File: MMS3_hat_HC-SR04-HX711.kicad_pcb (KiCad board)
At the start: 2 copper layers, 100 x 50 mm, 64 parts, among them J1 Chainbus in, J10 Conn_01x04_Pin, J11 Conn_01x04_Pin, J2 Chainbus Out, J3 Conn_01x04_Pin, J4 Debug_USART_TX, J5 Conn_01x04_Pin, J6 Conn_01x04_Pin, J7 Program, J8 Conn_01x04_Pin, J9 Conn_01x04_Pin, Q1 MMBT3906, U1 SN74CB3Q3384APW, U2 M24C64, U3 AMS1117, U4 CH32V003FxPx, U5 HX711

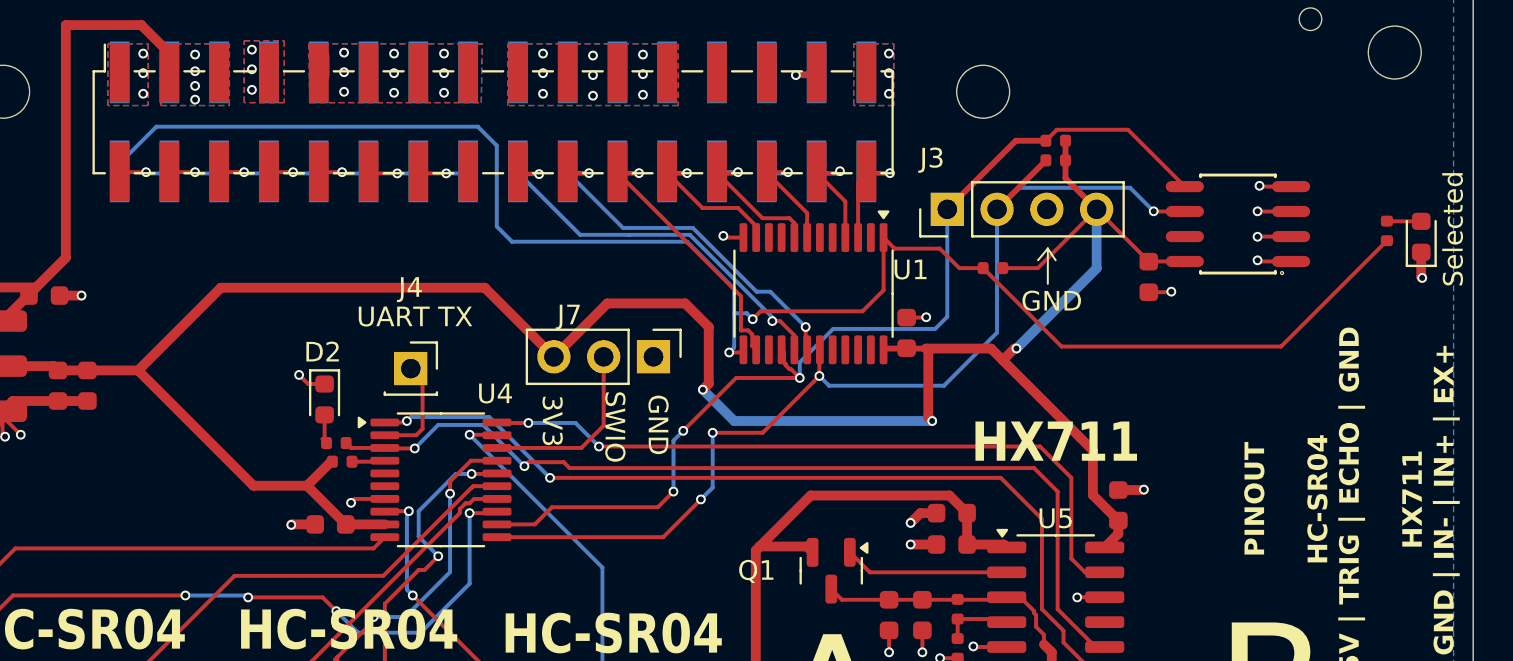
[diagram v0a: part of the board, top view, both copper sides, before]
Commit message: updated bus switch to sensible one
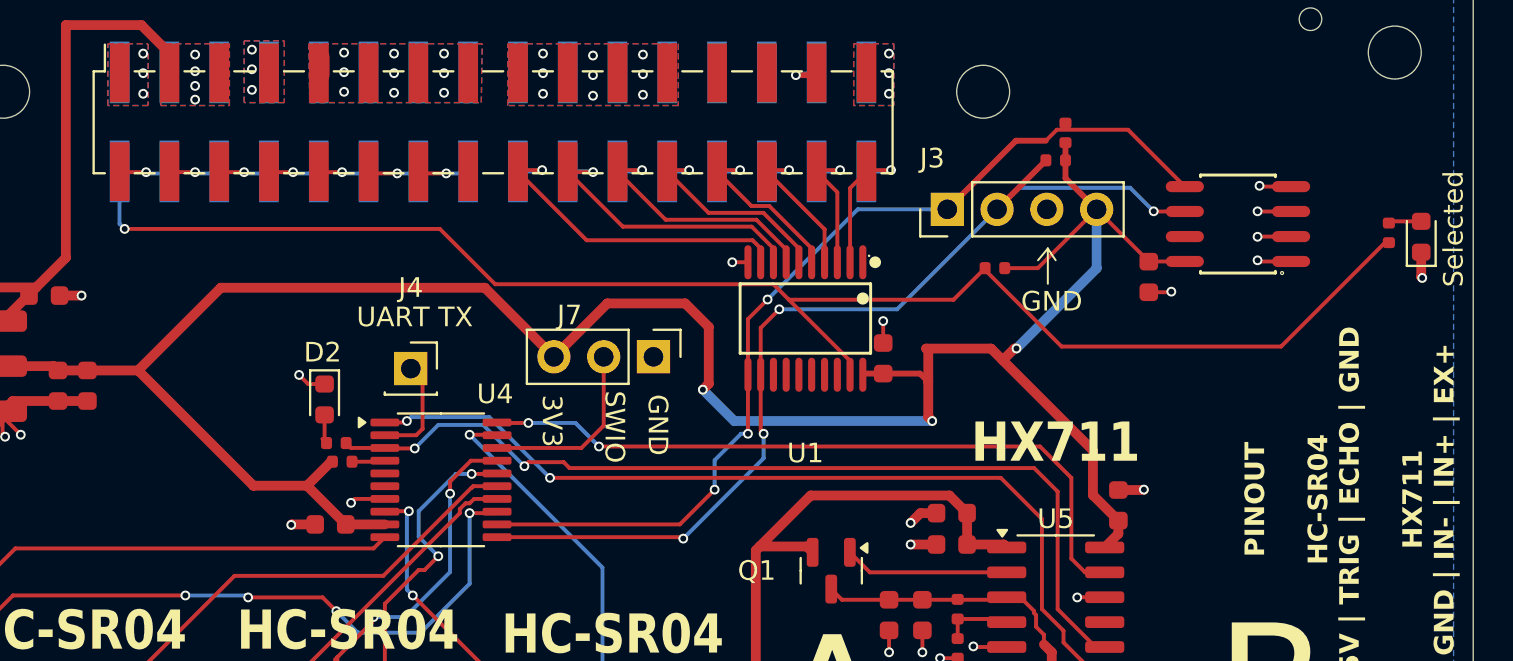
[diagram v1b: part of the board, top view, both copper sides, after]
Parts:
- removed PN1: ~, PCM_JLCPCB:Part_Num_JLCPCB
- removed R2, R3, R4: 10kΩ, PCM_JLCPCB:R_0402
- added R25: 10kΩ, PCM_JLCPCB:R_0402, F.Cu at (157.2, 96.1)
- added R27: 330Ω, PCM_JLCPCB:R_0402, F.Cu at (173.7, 101.2)
- added R9: 10kΩ, PCM_JLCPCB:R_0402, F.Cu at (156.7, 97.5)
- R1: value 330Ω -> 10kΩ
- U1: value SN74CB3Q3384APW -> SN74CB3Q3245PWR; footprint Package_SO:TSSOP-24_4.4x7.8mm_P0.65mm -> SN74CB3Q3245PWR:TSSOP-20_L6.5-W4.4-P0.65-LS6.4-BL
- moved R1 20.1 mm to (153.6, 103.0), turned to 0 degrees
- moved C1 1.76 mm to (147.9, 107.6)
- moved U1 1.33 mm to (143.9, 105.6), turned to 180 degrees
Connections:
- R1 pad 2: Net-(D1-A) -> +3V3
- U1 pad 1: /Bus_switch/SEL1 -> unconnected-(U1-NC-Pad1)
- U1 pad 10: /Bus_switch/Chainbus.SCK -> GND
- U1 pad 11: /Bus_switch/Chainbus_In.SCK -> /Bus_switch/Chainbus.SDA
- U1 pad 12: GND -> /Bus_switch/Chainbus.SCL
- U1 pad 13: /Bus_switch/SEL1 -> /Bus_switch/Chainbus.CS
- U1 pad 14: /Bus_switch/Chainbus_In.CS -> /Bus_switch/Chainbus.SCK
- U1 pad 15: /Bus_switch/Chainbus.CS -> /Bus_switch/Chainbus.MOSI
- U1 pad 16: /Bus_switch/Chainbus.SDA -> /Bus_switch/Chainbus.MISO
- U1 pad 17: /Bus_switch/Chainbus_In.SDA -> /Bus_switch/Chainbus.TX
- U1 pad 18: /Bus_switch/Chainbus_In.SCL -> /Bus_switch/Chainbus.RX
- U1 pad 19: /Bus_switch/Chainbus.SCL -> /Bus_switch/SEL1
- U1 pad 2: /Bus_switch/Chainbus.RX -> /Bus_switch/Chainbus_In.RX
- U1 pad 20: unconnected-(U1-2B4-Pad20) -> +3V3
- U1 pad 3: /Bus_switch/Chainbus_In.RX -> /Bus_switch/Chainbus_In.TX
- U1 pad 4: /Bus_switch/Chainbus_In.TX -> /Bus_switch/Chainbus_In.MISO
- U1 pad 5: /Bus_switch/Chainbus.TX -> /Bus_switch/Chainbus_In.MOSI
- U1 pad 6: /Bus_switch/Chainbus.MISO -> /Bus_switch/Chainbus_In.SCK
- U1 pad 7: /Bus_switch/Chainbus_In.MISO -> /Bus_switch/Chainbus_In.CS
- U1 pad 8: /Bus_switch/Chainbus_In.MOSI -> /Bus_switch/Chainbus_In.SCL
- U1 pad 9: /Bus_switch/Chainbus.MOSI -> /Bus_switch/Chainbus_In.SDA
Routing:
- net /Bus_switch/SEL1: track 83.9 -> 78.8 mm, vias 2 -> 1
- net /Bus_switch/Chainbus_In.SCL: track 18.6 -> 15.4 mm, vias 2 -> 1
- net /Bus_switch/Chainbus_In.SCK: track 8.13 -> 11.3 mm
- net /Bus_switch/Chainbus_In.SDA: track 20.4 -> 17.2 mm, vias 2 -> 1
- net /Bus_switch/Chainbus.SCL: track 53.6 -> 50.7 mm
- net /Bus_switch/Chainbus.SDA: track 51.7 -> 48.9 mm
- net /Bus_switch/Chainbus_In.MISO: track 6.22 -> 8.17 mm
- net /Bus_switch/Chainbus_In.MOSI: track 7.79 -> 9.56 mm
- net /Bus_switch/Chainbus_In.RX: track 5.78 -> 7.54 mm
- net +3V3: track 128.3 -> 129.6 mm
- net /Bus_switch/Chainbus_In.TX: track 6.24 -> 7.51 mm
- net /Bus_switch/Chainbus_In.CS: track 14.2 -> 13.5 mm
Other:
- board text added: "3"
- board text removed: "2"

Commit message: rounded da corners
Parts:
- moved H9 2.05 mm to (86.0, 91.0)
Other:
- outline, holes or cut-outs redrawn
- board text added: "Front and Back keepout zone for DIN rail mount"
- board text added: "Version 1.0 Made by Wojciech Szafrański"
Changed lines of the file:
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@@
 	(footprint "PCM_JLCPCB:Hole_Tooling_JLCPCB"
 		(layer "F.Cu")
-		(at 85.337849 89.057177)
+		(at 86 91)
 		(property "Reference" "H9"
 			(at 0 -0.5 0)
@@
 			(polygon
 				(pts
-					(xy 84.337849 88.057177) (xy 86.337849 88.057177) (xy 86.337849 90.057177) (xy 84.337849 90.057177)
+					(xy 85 90) (xy 87 90) (xy 87 92) (xy 85 92)
 				)
 			)
@@
 		(layer "B.SilkS")
 	)
-	(gr_rect
+	(gr_line
+		(start 178 88)
+		(end 178 96)
+		(stroke
+			(width 0.3)
+			(type solid)
+		)
+		(layer "Eco1.User")
+	)
+	(gr_line
+		(start 86 91)
+		(end 170 91)
+		(stroke
+			(width 0.3)
+			(type solid)
+		)
+		(layer "Eco1.User")
+	)
+	(gr_line
+		(start 78 96)
+		(end 81 96)
+		(stroke
+			(width 0.3)
+			(type solid)
+		)
+		(layer "Eco1.User")
+	)
+	(gr_line
+		(start 180 86)
+		(end 180 82)
+		(stroke
+			(width 0.5)
+			(type solid)
+		)
+		(layer "Eco1.User")
+	)
+	(gr_line
+		(start 175 96)
+		(end 170 91)
+		(stroke
+			(width 0.3)
+			(type solid)
+		)
+		(layer "Eco1.User")
+	)
+	(gr_line
+		(start 186 81)
+		(end 180 86)
+		(stroke
+			(width 0.5)
+			(type solid)
+		)
+		(layer "Eco1.User")
+	)
+	(gr_line
+		(start 184 86)
+		(end 180 86)
+		(stroke
+			(width 0.5)
+			(type solid)
+		)
+		(layer "Eco1.User")
+	)
+	(gr_line
 		(start 78 88)
-		(end 178 138)
+		(end 78 96)
 		(stroke
-			(width 0.01)
+			(width 0.3)
 			(type solid)
 		)
-		(fill no)
+		(layer "Eco1.User")
+	)
+	(gr_line
+		(start 81 96)
+		(end 86 91)
+		(stroke
+			(width 0.3)
+			(type solid)
+		)
+		(layer "Eco1.User")
+	)
+	(gr_line
+		(start 178 96)
+		(end 175 96)
+		(stroke
+			(width 0.3)
+			(type solid)
+		)
+		(layer "Eco1.User")
+	)
+	(gr_line
+		(start 178 88)
+		(end 78 88)
+		(stroke
+			(width 0.3)
+			(type solid)
+		)
+		(layer "Eco1.User")
+	)
+	(gr_arc
+		(start 174 88)
+		(mid 176.828427 89.171573)
+		(end 178 92)
+		(stroke
+			(width 0.05)
+			(type default)
+		)
+		(layer "Edge.Cuts")
+	)
+	(gr_arc
+		(start 178 134)
+		(mid 176.828427 136.828427)
+		(end 174 138)
+		(stroke
+			(width 0.05)
+			(type default)
+		)
+		(layer "Edge.Cuts")
+	)
+	(gr_line
+		(start 174 138)
+		(end 82 138)
+		(stroke
+			(width 0.05)
+			(type default)
+		)
+		(layer "Edge.Cuts")
+	)
+	(gr_line
+		(start 178 92)
+		(end 178 134)
+		(stroke
+			(width 0.05)
+			(type default)
+		)
+		(layer "Edge.Cuts")
+	)
+	(gr_line
+		(start 82 88)
+		(end 174 88)
+		(stroke
+			(width 0.05)
+			(type default)
+		)
+		(layer "Edge.Cuts")
+	)
+	(gr_arc
+		(start 82 138)
+		(mid 79.171573 136.828427)
+		(end 78 134)
+		(stroke
+			(width 0.05)
+			(type default)
+		)
+		(layer "Edge.Cuts")
+	)
+	(gr_line
+		(start 78 134)
+		(end 78 92)
+		(stroke
+			(width 0.05)
+			(type default)
+		)
+		(layer "Edge.Cuts")
+	)
+	(gr_arc
+		(start 78 92)
+		(mid 79.171573 89.171573)
+		(end 82 88)
+		(stroke
+			(width 0.05)
+			(type default)
+		)
 		(layer "Edge.Cuts")
 	)
@@
 		)
 	)
+	(gr_text "Version 1.0\nMade by\nWojciech Szafrański"
+		(at 91 97 0)
+		(layer "F.SilkS")
+		(effects
+			(font
+				(size 1 1)
+				(thickness 0.2)
+				(bold yes)
+			)
+		)
+	)
 	(gr_text "GND"
 		(at 138.7 127.2 270)
@@
 		)
 	)
+	(gr_text "Front and Back keepout\nzone for DIN rail mount"
+		(at 182 79 0)
+		(layer "Eco1.User")
+		(effects
+			(font
+				(size 1 1)
+				(thickness 0.2)
+				(bold yes)
+			)
+			(justify left bottom)
+		)
+	)
